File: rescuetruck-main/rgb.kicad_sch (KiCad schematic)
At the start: 96 parts

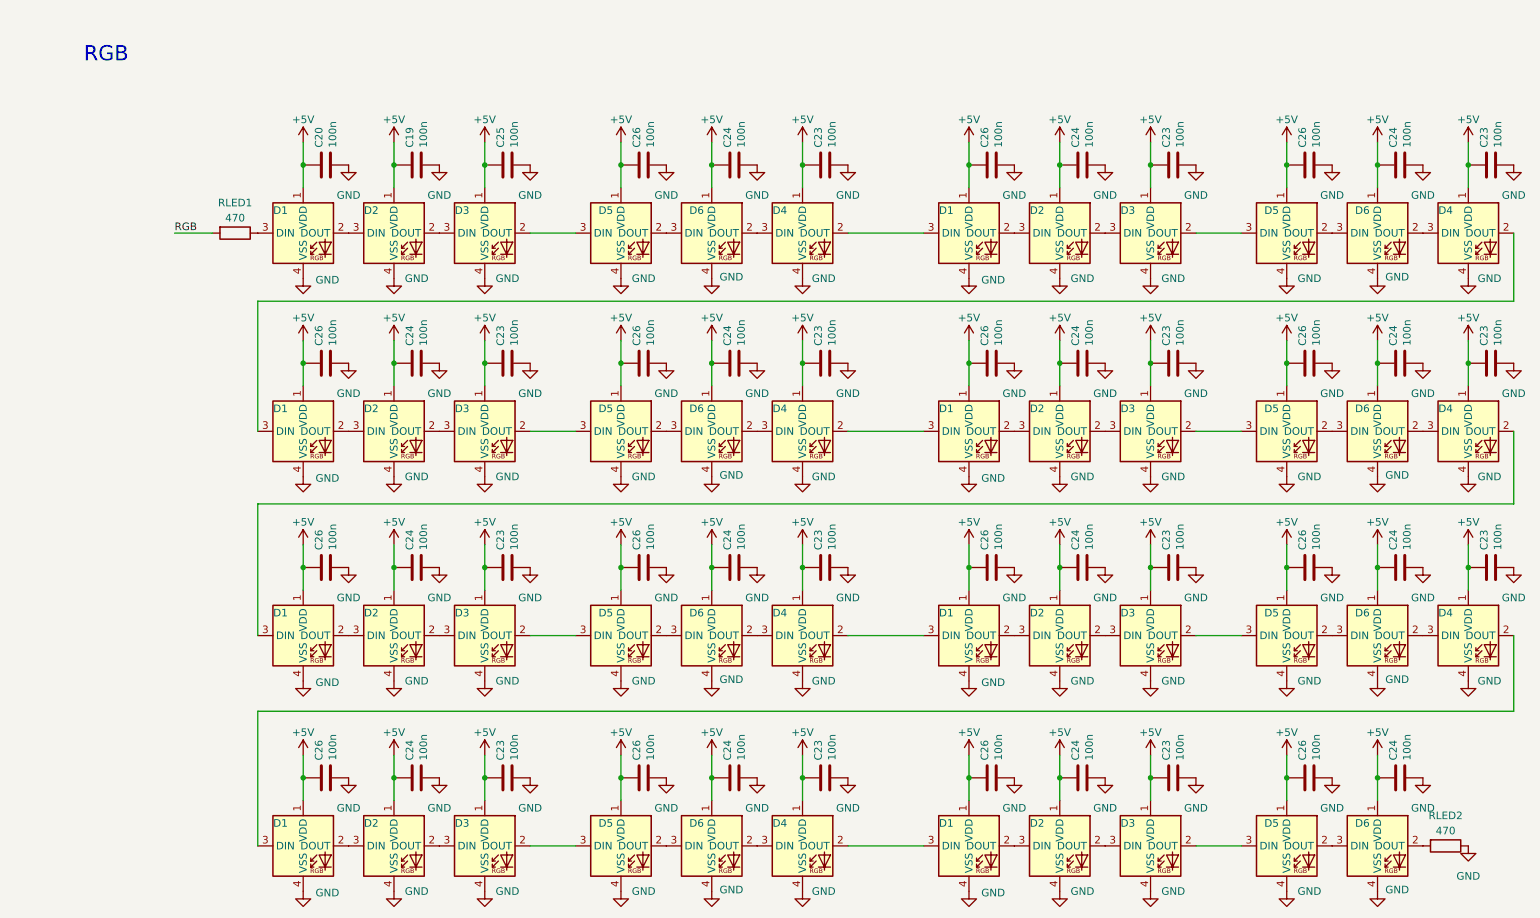
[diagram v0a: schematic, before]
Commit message: deleted caps, res from moon project
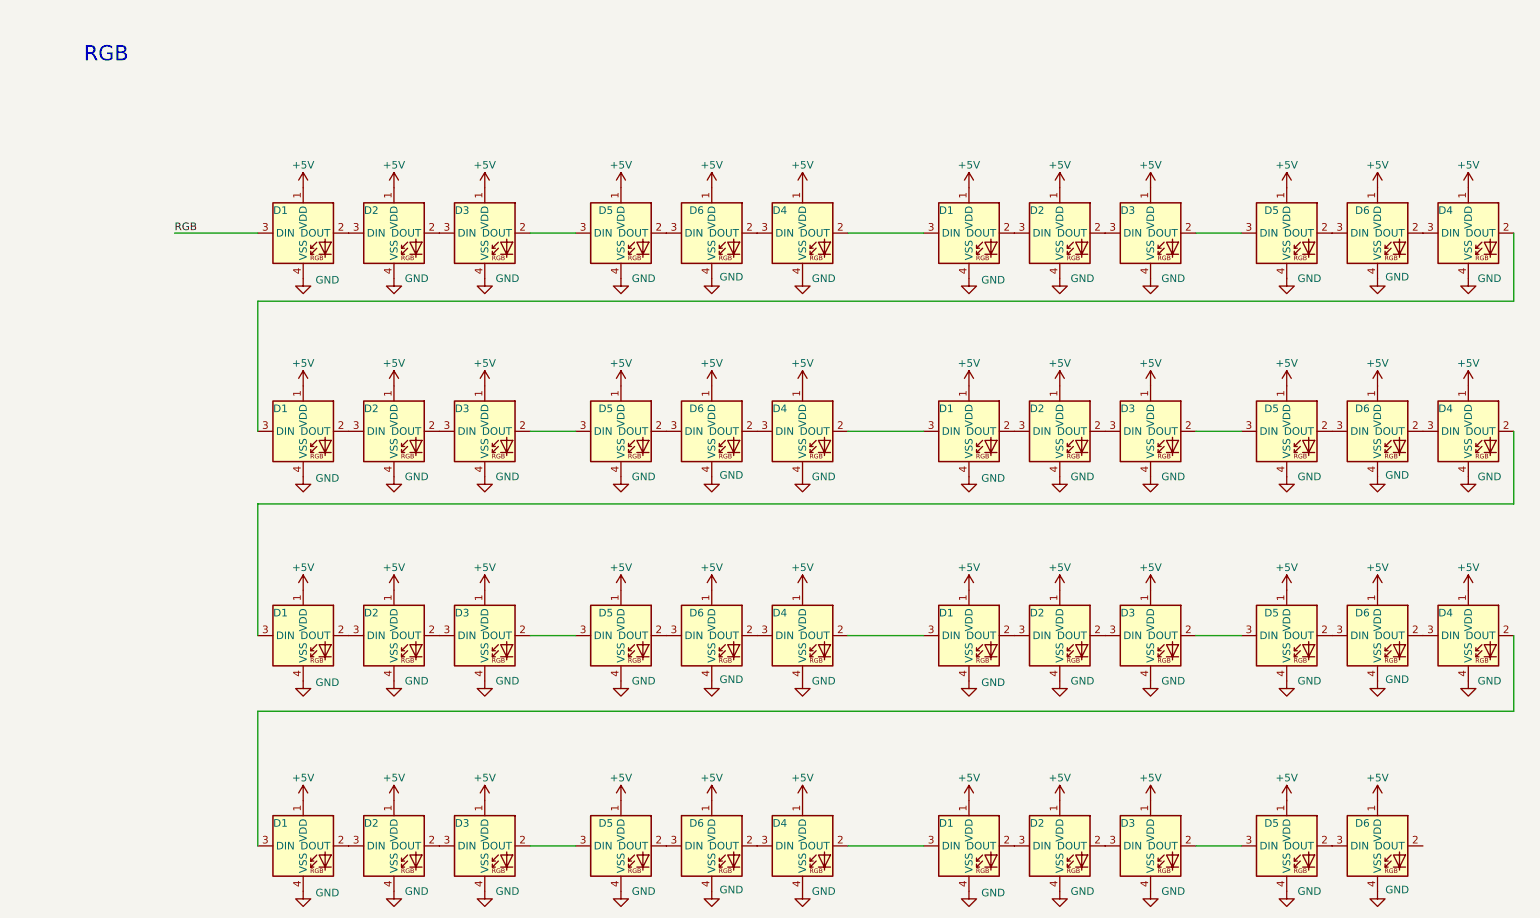
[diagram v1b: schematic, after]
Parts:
- removed C19, C20, C23 (x14), C24 (x15), C25, C26 (x15): 100n, Capacitor_SMD:C_0402_1005Metric, symbol Device:C
- removed RLED1, RLED2: 470, Resistor_SMD:R_0402_1005Metric, symbol Device:R
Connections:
- net RGB: now also D1.3 (DIN)

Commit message: vootvan progress
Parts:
- added C18: 100nF, Capacitor_SMD:C_0402_1005Metric, symbol Device:C_Small
- added U5: 74AHCT1G125, Package_TO_SOT_SMD:TSOT-23-5, symbol 74xGxx:74AHCT1G125
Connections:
- net +5V: now also C18.2, U5.5 (VCC)
- net GND: now also C18.1, U5.1, U5.3 (GND)
- net RGB: now also D4.3 (DIN), U5.4; no longer D1.3 (DIN)
- net at D4.2 (DOUT): now also D6.3 (DIN); no longer D1.3 (DIN) (x3)
- net at D4.3 (DIN): now also D1.2 (DOUT); no longer D6.2 (DOUT) (x4)
- net at D3.2 (DOUT): now also D2.3 (DIN); no longer D5.3 (DIN) (x3)
- net at D3.3 (DIN): now also D5.2 (DOUT); no longer D2.2 (DOUT) (x3)
- net at D5.2 (DOUT): now also D3.3 (DIN); no longer D6.3 (DIN) (x4)
- net at D5.3 (DIN): now also D6.2 (DOUT); no longer D3.2 (DOUT) (x4)
- net at D1.2 (DOUT): now also D6.3 (DIN); no longer D2.3 (DIN)
- net at D6.3 (DIN): now also D4.2 (DOUT); no longer D5.2 (DOUT) (x3)
- net at D6.2 (DOUT): now also D5.3 (DIN); no longer D4.3 (DIN) (x3)
- net at D2.2 (DOUT): now also D1.3 (DIN); no longer D3.3 (DIN) (x5)
- net at D2.3 (DIN): now also D3.2 (DOUT); no longer D1.2 (DOUT) (x4)
- net at D1.2 (DOUT): now also D4.3 (DIN); no longer D2.3 (DIN) (x2)
- net at D1.3 (DIN): now also D2.2 (DOUT); no longer D4.2 (DOUT) (x3)
- net at D1.2 (DOUT): no longer D2.3 (DIN)
- net at D6.2 (DOUT): now also D5.3 (DIN)
- new net: D2.3 (DIN), D3.2 (DOUT)
- new net: D4.2 (DOUT), D6.3 (DIN)
- new net: D3.3 (DIN), D5.2 (DOUT)
- new net RGB MCU: U5.2
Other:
- moved on the sheet: D1, D2, D3, D4, D5, D6
